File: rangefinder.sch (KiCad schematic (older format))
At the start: 5 parts, among them U9 VL53L0X

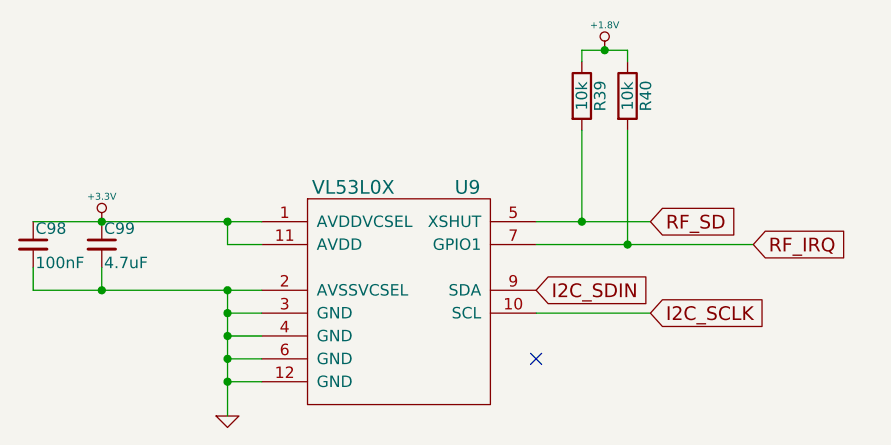
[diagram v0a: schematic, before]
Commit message: resolved ERC errors, and began assigning footprints
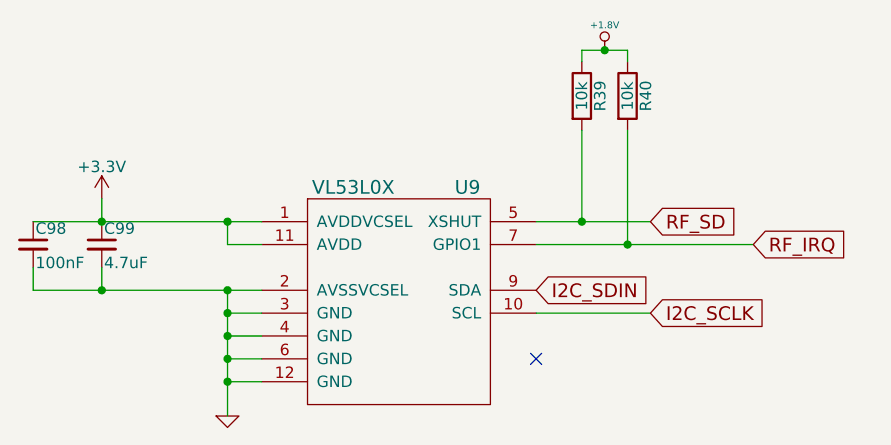
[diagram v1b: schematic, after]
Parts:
- C98: footprint (none) -> Capacitors_SMD:C_0603
- C99: footprint (none) -> Capacitors_SMD:C_0805
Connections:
- net +3.3V renamed +3V3
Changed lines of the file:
@@
 LIBS:N25Q128A
 LIBS:sparkfun
+LIBS:GSB3211311WEU
+LIBS:48258-0001
+LIBS:ArduinoSpecAn-cache
+LIBS:passiveelectret
+LIBS:passiveind
+LIBS:passiveinductor
+LIBS:fb_powerout
+LIBS:ferrite
+LIBS:df_device
 EELAYER 25 0
 EELAYER END
@@
 F 0 "U9" H 5600 4250 60  0000 C CNN
 F 1 "VL53L0X" H 5100 4250 60  0000 C CNN
-F 2 "" H 5350 3650 60  0000 C CNN
+F 2 "" H 5350 3650 60  0001 C CNN
 F 3 "" H 5350 3650 60  0000 C CNN
 	1    5300 3700
@@
 NoConn ~ 5900 3900
 $Comp
-L GND-RESCUE-DFTBoard #PWR096
+L GND-RESCUE-DFTBoard #PWR0100
 U 1 1 58598433
 P 4550 4150
-F 0 "#PWR096" H 4550 4150 30  0001 C CNN
+F 0 "#PWR0100" H 4550 4150 30  0001 C CNN
 F 1 "GND" H 4550 4080 30  0001 C CNN
 F 2 "" H 4550 4150 60  0001 C CNN
@@
 F 0 "C99" H 4010 3470 50  0000 L CNN
 F 1 "4.7uF" H 4010 3320 50  0000 L CNN
-F 2 "" H 4000 3400 50  0000 C CNN
+F 2 "Capacitors_SMD:C_0805" H 4000 3400 50  0001 C CNN
 F 3 "" H 4000 3400 50  0000 C CNN
 	1    4000 3400
@@
 F 0 "C98" H 3710 3470 50  0000 L CNN
 F 1 "100nF" H 3710 3320 50  0000 L CNN
-F 2 "" H 3700 3400 50  0000 C CNN
+F 2 "Capacitors_SMD:C_0603" H 3700 3400 50  0001 C CNN
 F 3 "" H 3700 3400 50  0000 C CNN
 	1    3700 3400
@@
 	4550 3400 4550 3300
 Connection ~ 4550 3300
-$Comp
-L +3.3V-RESCUE-DFTBoard #PWR097
-U 1 1 58598633
-P 4000 3300
-F 0 "#PWR097" H 4000 3260 30  0001 C CNN
-F 1 "+3.3V" H 4000 3410 30  0000 C CNN
-F 2 "" H 4000 3300 60  0001 C CNN
-F 3 "" H 4000 3300 60  0001 C CNN
-	1    4000 3300
-	1    0    0    -1
-$EndComp
 Text GLabel 6400 3300 2    60   Input ~ 0
 RF_SD
@@
 F 0 "R39" V 6180 2750 50  0000 C CNN
 F 1 "10k" V 6100 2750 50  0000 C CNN
-F 2 "" V 6030 2750 50  0000 C CNN
+F 2 "" V 6030 2750 50  0001 C CNN
 F 3 "" H 6100 2750 50  0000 C CNN
 	1    6100 2750
@@
 F 0 "R40" V 6380 2750 50  0000 C CNN
 F 1 "10k" V 6300 2750 50  0000 C CNN
-F 2 "" V 6230 2750 50  0000 C CNN
+F 2 "" V 6230 2750 50  0001 C CNN
 F 3 "" H 6300 2750 50  0000 C CNN
 	1    6300 2750
@@
 	5900 3300 6400 3300
 $Comp
-L +1.8V #PWR098
+L +1.8V #PWR0101
 U 1 1 585987BD
 P 6200 2550
-F 0 "#PWR098" H 6200 2690 20  0001 C CNN
+F 0 "#PWR0101" H 6200 2690 20  0001 C CNN
 F 1 "+1.8V" H 6200 2660 30  0000 C CNN
 F 2 "" H 6200 2550 60  0001 C CNN
@@
 Text GLabel 6850 3400 2    60   Input ~ 0
 RF_IRQ
+$Comp
+L +3.3V #PWR0102
+U 1 1 587438B2
+P 4000 3200
+F 0 "#PWR0102" H 4000 3050 50  0001 C CNN
+F 1 "+3.3V" H 4000 3340 50  0000 C CNN
+F 2 "" H 4000 3200 50  0000 C CNN
+F 3 "" H 4000 3200 50  0000 C CNN
+	1    4000 3200
+	1    0    0    -1
+$EndComp
+Wire Wire Line
+	4000 3200 4000 3300
 $EndSCHEMATC

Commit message: A few more footprints
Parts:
- U9: footprint (none) -> lga12:LGA12
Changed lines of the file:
@@
 F 0 "U9" H 5600 4250 60  0000 C CNN
 F 1 "VL53L0X" H 5100 4250 60  0000 C CNN
-F 2 "" H 5350 3650 60  0001 C CNN
+F 2 "lga12:LGA12" H 5350 3650 60  0001 C CNN
 F 3 "" H 5350 3650 60  0000 C CNN
 	1    5300 3700

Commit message: added resistor footprints (1206)
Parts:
- R39, R40: footprint (none) -> Resistors_SMD:R_1206
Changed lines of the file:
@@
 F 0 "R39" V 6180 2750 50  0000 C CNN
 F 1 "10k" V 6100 2750 50  0000 C CNN
-F 2 "" V 6030 2750 50  0001 C CNN
+F 2 "Resistors_SMD:R_1206" V 6030 2750 50  0001 C CNN
 F 3 "" H 6100 2750 50  0000 C CNN
 	1    6100 2750
@@
 F 0 "R40" V 6380 2750 50  0000 C CNN
 F 1 "10k" V 6300 2750 50  0000 C CNN
-F 2 "" V 6230 2750 50  0001 C CNN
+F 2 "Resistors_SMD:R_1206" V 6230 2750 50  0001 C CNN
 F 3 "" H 6300 2750 50  0000 C CNN
 	1    6300 2750

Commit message: fixed a few diagram/footprint pin mismatches, getting ready to pull gene's microhdmi footprint
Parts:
- U9: footprint lga12:LGA12 -> DFTcustom:LGA12
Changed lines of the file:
@@
 LIBS:ferrite
 LIBS:df_device
+LIBS:JACK_TRS_5PINS
 EELAYER 25 0
 EELAYER END
@@
 F 0 "U9" H 5600 4250 60  0000 C CNN
 F 1 "VL53L0X" H 5100 4250 60  0000 C CNN
-F 2 "lga12:LGA12" H 5350 3650 60  0001 C CNN
+F 2 "DFTcustom:LGA12" H 5350 3650 60  0001 C CNN
 F 3 "" H 5350 3650 60  0000 C CNN
 	1    5300 3700

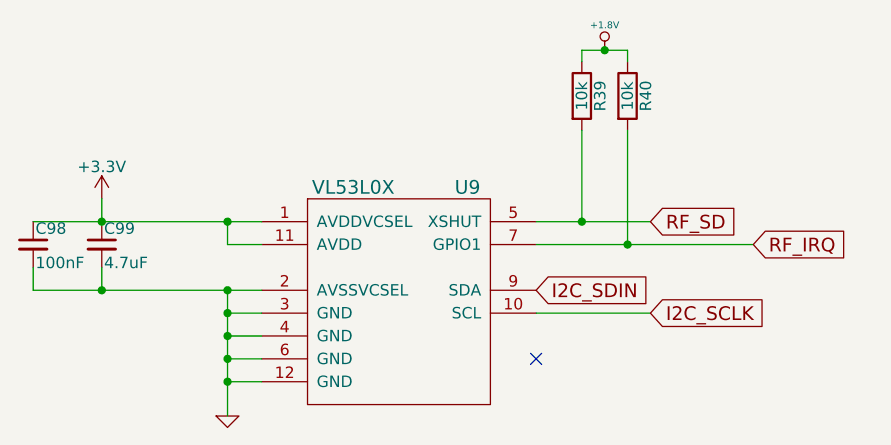
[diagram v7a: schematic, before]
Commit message: fixed all schematic/footprint errors
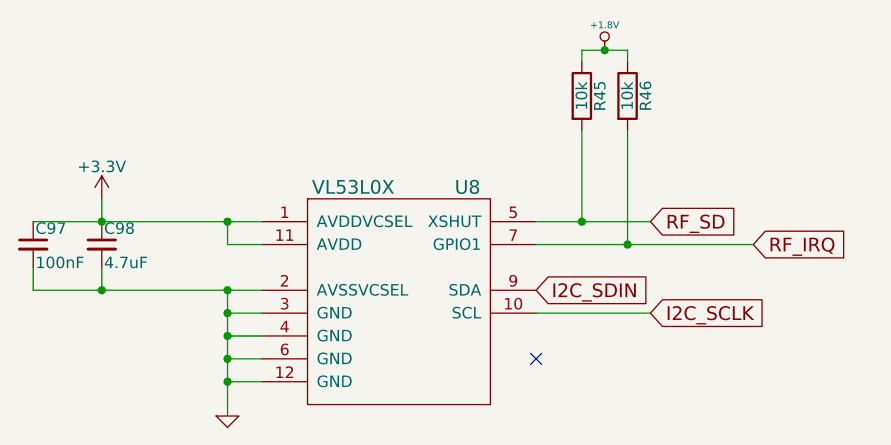
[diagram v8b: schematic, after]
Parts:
- renumbered C98 to C97, C99 to C98, R39 to R45, R40 to R46, U9 to U8
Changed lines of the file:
@@
 $EndDescr
 $Comp
-L VL53L0X U9
+L VL53L0X U8
 U 1 1 58530049
 P 5300 3700
-F 0 "U9" H 5600 4250 60  0000 C CNN
+F 0 "U8" H 5600 4250 60  0000 C CNN
 F 1 "VL53L0X" H 5100 4250 60  0000 C CNN
 F 2 "DFTcustom:LGA12" H 5350 3650 60  0001 C CNN
@@
 Connection ~ 4550 3700
 $Comp
-L C_Small C99
+L C_Small C98
 U 1 1 585984E0
 P 4000 3400
-F 0 "C99" H 4010 3470 50  0000 L CNN
+F 0 "C98" H 4010 3470 50  0000 L CNN
 F 1 "4.7uF" H 4010 3320 50  0000 L CNN
 F 2 "Capacitors_SMD:C_0805" H 4000 3400 50  0001 C CNN
@@
 $EndComp
 $Comp
-L C_Small C98
+L C_Small C97
 U 1 1 58598585
 P 3700 3400
-F 0 "C98" H 3710 3470 50  0000 L CNN
+F 0 "C97" H 3710 3470 50  0000 L CNN
 F 1 "100nF" H 3710 3320 50  0000 L CNN
 F 2 "Capacitors_SMD:C_0603" H 3700 3400 50  0001 C CNN
@@
 RF_SD
 $Comp
-L R R39
+L R R45
 U 1 1 58598665
 P 6100 2750
-F 0 "R39" V 6180 2750 50  0000 C CNN
+F 0 "R45" V 6180 2750 50  0000 C CNN
 F 1 "10k" V 6100 2750 50  0000 C CNN
 F 2 "Resistors_SMD:R_1206" V 6030 2750 50  0001 C CNN
@@
 $EndComp
 $Comp
-L R R40
+L R R46
 U 1 1 585986E0
 P 6300 2750
-F 0 "R40" V 6380 2750 50  0000 C CNN
+F 0 "R46" V 6380 2750 50  0000 C CNN
 F 1 "10k" V 6300 2750 50  0000 C CNN
 F 2 "Resistors_SMD:R_1206" V 6230 2750 50  0001 C CNN
